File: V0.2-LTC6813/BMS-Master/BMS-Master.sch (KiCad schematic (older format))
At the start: 26 parts

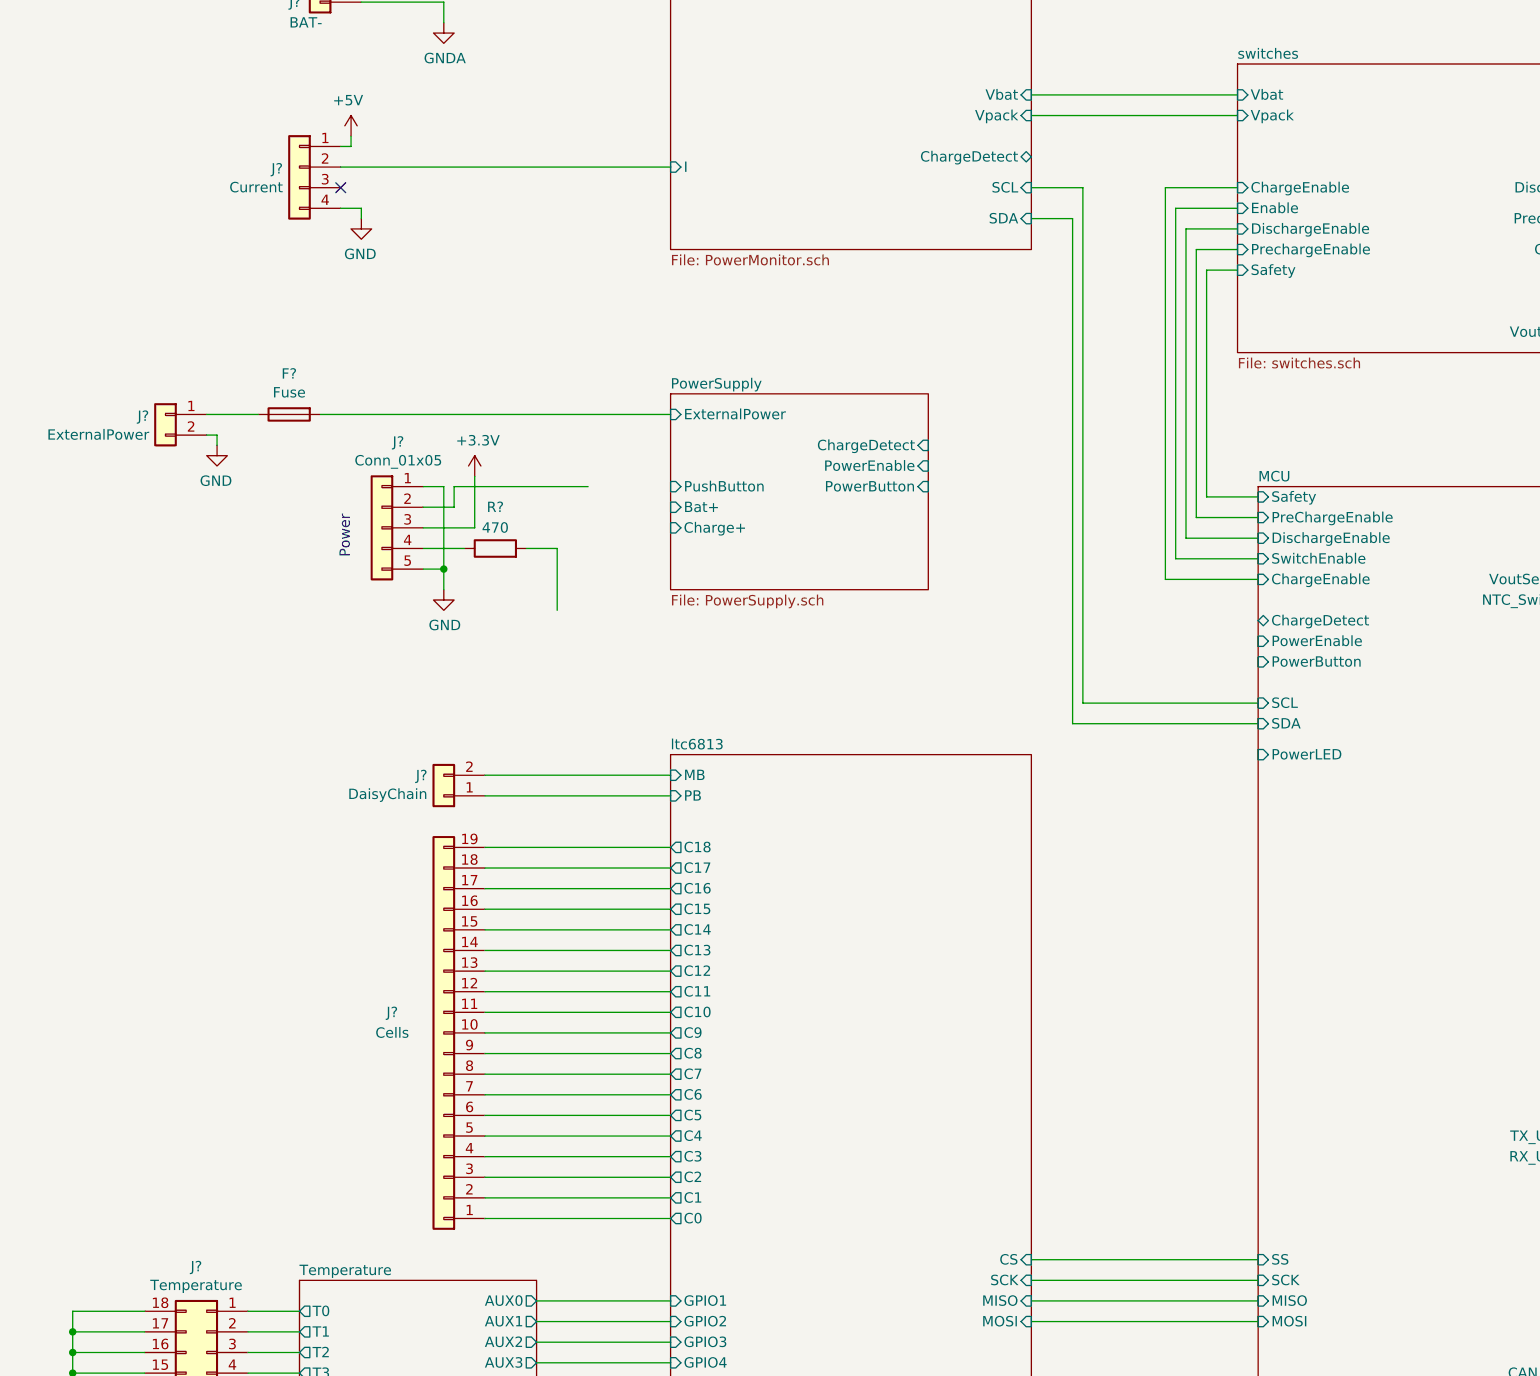
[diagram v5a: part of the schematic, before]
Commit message: Schematics 85% completed
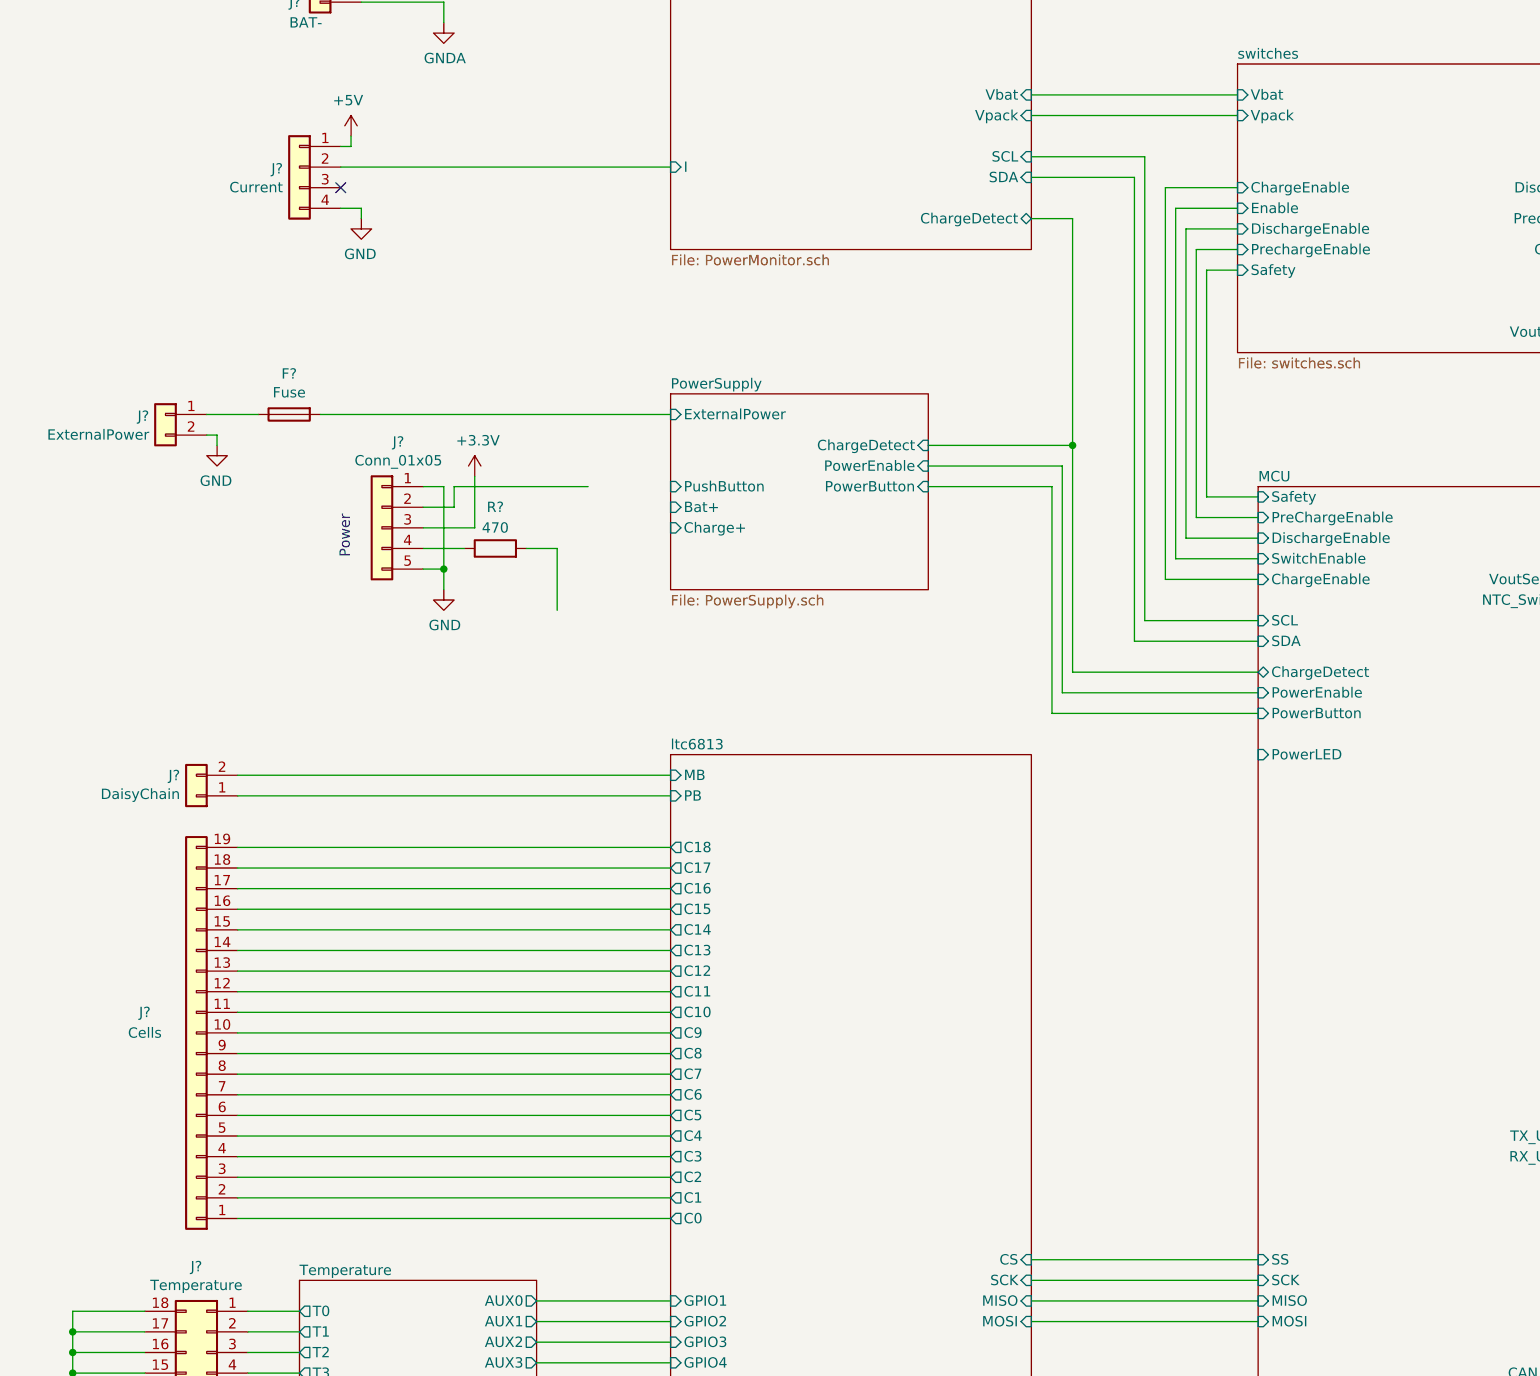
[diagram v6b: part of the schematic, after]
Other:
- moved on the sheet: DaisyChain, J?
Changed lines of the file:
@@
 L BMS-Master-rescue:Conn_01x02-Connector_Generic DaisyChain
 U 1 1 5C30CF47
-P 3250 5150
-F 0 "DaisyChain" H 3329 5142 50  0000 L CNN
-F 1 "J?" H 3329 5051 50  0000 L CNN
-F 2 "" H 3250 5150 50  0001 C CNN
-F 3 "~" H 3250 5150 50  0001 C CNN
-	1    3250 5150
+P 2050 5150
+F 0 "DaisyChain" H 2129 5142 50  0000 L CNN
+F 1 "J?" H 2129 5051 50  0000 L CNN
+F 2 "" H 2050 5150 50  0001 C CNN
+F 3 "~" H 2050 5150 50  0001 C CNN
+	1    2050 5150
 	-1   0    0    1
 $EndComp
 Wire Wire Line
-	4350 5150 3450 5150
-Wire Wire Line
-	3450 5050 4350 5050
+	4350 5150 2250 5150
+Wire Wire Line
+	2250 5050 4350 5050
 Wire Wire Line
 	10000 10300 10000 9450
@@
 F1 "PowerMonitor.sch" 50
 F2 "I" I L 4350 2100 50
-F3 "SCL" I R 6100 2200 50
-F4 "SDA" I R 6100 2350 50
+F3 "SCL" I R 6100 2050 50
+F4 "SDA" I R 6100 2150 50
 F5 "BAT+" I L 4350 900 50
 F6 "Charge+" I R 6100 950 50
@@
 F8 "Vbat" I R 6100 1750 50
 F9 "Vpack" I R 6100 1850 50
-F10 "ChargeDetect" B R 6100 2050 50
+F10 "ChargeDetect" B R 6100 2350 50
 $EndSheet
 NoConn ~ 2750 2200
@@
 L Connector_Generic:Conn_01x19 J?
 U 1 1 5C915AF7
-P 3250 6300
-F 0 "J?" H 3500 6200 50  0000 C CNN
-F 1 "Cells" H 3500 6300 50  0000 C CNN
-F 2 "" H 3250 6300 50  0001 C CNN
-F 3 "~" H 3250 6300 50  0001 C CNN
-	1    3250 6300
+P 2050 6300
+F 0 "J?" H 2300 6200 50  0000 C CNN
+F 1 "Cells" H 2300 6300 50  0000 C CNN
+F 2 "" H 2050 6300 50  0001 C CNN
+F 3 "~" H 2050 6300 50  0001 C CNN
+	1    2050 6300
 	-1   0    0    1
 $EndComp
 Wire Wire Line
-	3450 7200 4350 7200
-Wire Wire Line
-	4350 7100 3450 7100
-Wire Wire Line
-	3450 7000 4350 7000
-Wire Wire Line
-	4350 6900 3450 6900
-Wire Wire Line
-	3450 6800 4350 6800
-Wire Wire Line
-	4350 6700 3450 6700
-Wire Wire Line
-	3450 6600 4350 6600
-Wire Wire Line
-	4350 6500 3450 6500
-Wire Wire Line
-	3450 6400 4350 6400
-Wire Wire Line
-	4350 6300 3450 6300
-Wire Wire Line
-	3450 6200 4350 6200
-Wire Wire Line
-	4350 6100 3450 6100
-Wire Wire Line
-	3450 6000 4350 6000
-Wire Wire Line
-	4350 5900 3450 5900
-Wire Wire Line
-	3450 5800 4350 5800
-Wire Wire Line
-	4350 5700 3450 5700
-Wire Wire Line
-	3450 5600 4350 5600
-Wire Wire Line
-	4350 5500 3450 5500
-Wire Wire Line
-	3450 5400 4350 5400
+	2250 7200 4350 7200
+Wire Wire Line
+	4350 7100 2250 7100
+Wire Wire Line
+	2250 7000 4350 7000
+Wire Wire Line
+	4350 6900 2250 6900
+Wire Wire Line
+	2250 6800 4350 6800
+Wire Wire Line
+	4350 6700 2250 6700
+Wire Wire Line
+	2250 6600 4350 6600
+Wire Wire Line
+	4350 6500 2250 6500
+Wire Wire Line
+	2250 6400 4350 6400
+Wire Wire Line
+	4350 6300 2250 6300
+Wire Wire Line
+	2250 6200 4350 6200
+Wire Wire Line
+	4350 6100 2250 6100
+Wire Wire Line
+	2250 6000 4350 6000
+Wire Wire Line
+	4350 5900 2250 5900
+Wire Wire Line
+	2250 5800 4350 5800
+Wire Wire Line
+	4350 5700 2250 5700
+Wire Wire Line
+	2250 5600 4350 5600
+Wire Wire Line
+	4350 5500 2250 5500
+Wire Wire Line
+	2250 5400 4350 5400
 $Comp
 L power:GNDA #PWR?
@@
 F0 "MCU" 50
 F1 "MCU.sch" 50
-F2 "ChargeDetect" B L 7200 4300 50
+F2 "ChargeDetect" B L 7200 4550 50
 F3 "PreChargeEnable" I L 7200 3800 50
 F4 "DischargeEnable" I L 7200 3900 50
-F5 "PowerEnable" I L 7200 4400 50
-F6 "PowerButton" I L 7200 4500 50
+F5 "PowerEnable" I L 7200 4650 50
+F6 "PowerButton" I L 7200 4750 50
 F7 "PowerLED" I L 7200 4950 50
 F8 "LED0" I L 7200 9800 50
@@
 F20 "MOSI" I L 7200 7700 50
 F21 "SPI_WT_SS" I L 7200 9000 50
-F22 "SCL" I L 7200 4700 50
-F23 "SDA" I L 7200 4800 50
+F22 "SCL" I L 7200 4300 50
+F23 "SDA" I L 7200 4400 50
 F24 "OLED_SCL" I R 8750 8900 50
 F25 "OLED_SDA" I R 8750 9000 50
@@
 	6750 4100 7200 4100
 Wire Wire Line
-	6100 2200 6350 2200
-Wire Wire Line
-	6350 2200 6350 4700
-Wire Wire Line
-	6350 4700 7200 4700
-Wire Wire Line
-	6300 2350 6300 4800
-Wire Wire Line
-	6300 4800 7200 4800
-Wire Wire Line
-	6100 2350 6300 2350
+	6100 2050 6650 2050
+Wire Wire Line
+	6650 2050 6650 4300
+Wire Wire Line
+	6650 4300 7200 4300
+Wire Wire Line
+	6600 4400 7200 4400
 Wire Wire Line
 	6100 1750 7100 1750
@@
 Wire Wire Line
 	3700 8550 4350 8550
+Wire Wire Line
+	6600 2150 6100 2150
+Wire Wire Line
+	6600 2150 6600 4400
+Wire Wire Line
+	6100 2350 6300 2350
+Wire Wire Line
+	6300 2350 6300 3450
+Wire Wire Line
+	6300 4550 7200 4550
+Wire Wire Line
+	5600 3450 6300 3450
+Connection ~ 6300 3450
+Wire Wire Line
+	6300 3450 6300 4550
+Wire Wire Line
+	5600 3550 6250 3550
+Wire Wire Line
+	6250 3550 6250 4650
+Wire Wire Line
+	6250 4650 7200 4650
+Wire Wire Line
+	7200 4750 6200 4750
+Wire Wire Line
+	6200 4750 6200 3650
+Wire Wire Line
+	6200 3650 5600 3650
 $EndSCHEMATC

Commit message: Schematics 90% completed
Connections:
- net MCU/PowerLED: now also R?.2
- net PowerSupply/PushButton: now also J?.2 (Pin_2)
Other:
- moved on the sheet: F?, J?, R?
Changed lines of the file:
@@
 L BMS-Master-rescue:Conn_01x05-Connector_Generic J?
 U 1 1 5ABE6776
-P 2950 3850
-F 0 "J?" H 2870 4267 50  0000 C CNN
-F 1 "Conn_01x05" H 2870 4176 50  0000 C CNN
-F 2 "" H 2950 3850 50  0001 C CNN
-F 3 "~" H 2950 3850 50  0001 C CNN
-	1    2950 3850
+P 2950 4000
+F 0 "J?" H 2870 4417 50  0000 C CNN
+F 1 "Conn_01x05" H 2870 4326 50  0000 C CNN
+F 2 "" H 2950 4000 50  0001 C CNN
+F 3 "~" H 2950 4000 50  0001 C CNN
+	1    2950 4000
 	-1   0    0    -1
 $EndComp
-Text Notes 2800 4000 1    50   ~ 0
+Text Notes 2800 4150 1    50   ~ 0
 Power
 $Comp
 L BMS-Master-rescue:+3.3V-power #PWR?
 U 1 1 5ABE6960
-P 3400 3600
-F 0 "#PWR?" H 3400 3450 50  0001 C CNN
-F 1 "+3.3V" H 3415 3773 50  0000 C CNN
-F 2 "" H 3400 3600 50  0001 C CNN
-F 3 "" H 3400 3600 50  0001 C CNN
-	1    3400 3600
+P 3400 3750
+F 0 "#PWR?" H 3400 3600 50  0001 C CNN
+F 1 "+3.3V" H 3415 3923 50  0000 C CNN
+F 2 "" H 3400 3750 50  0001 C CNN
+F 3 "" H 3400 3750 50  0001 C CNN
+	1    3400 3750
 	1    0    0    -1
 $EndComp
@@
 L BMS-Master-rescue:R-Device R?
 U 1 1 5ABEC8F7
-P 3500 3950
-F 0 "R?" V 3700 3950 50  0000 C CNN
-F 1 "470" V 3600 3950 50  0000 C CNN
-F 2 "Resistors_SMD:R_0603_HandSoldering" V 3430 3950 50  0001 C CNN
-F 3 "~" H 3500 3950 50  0001 C CNN
-	1    3500 3950
+P 3500 4100
+F 0 "R?" V 3700 4100 50  0000 C CNN
+F 1 "470" V 3600 4100 50  0000 C CNN
+F 2 "Resistors_SMD:R_0603_HandSoldering" V 3430 4100 50  0001 C CNN
+F 3 "~" H 3500 4100 50  0001 C CNN
+	1    3500 4100
 	0    -1   -1   0
 $EndComp
 Wire Wire Line
-	3150 3950 3350 3950
-Wire Wire Line
-	3650 3950 3800 3950
+	3150 4100 3350 4100
+Wire Wire Line
+	3650 4100 3800 4100
 $Comp
 L BMS-Master-rescue:GND-power #PWR?
 U 1 1 5ABF492B
-P 3250 4150
-F 0 "#PWR?" H 3250 3900 50  0001 C CNN
-F 1 "GND" H 3255 3977 50  0000 C CNN
-F 2 "" H 3250 4150 50  0001 C CNN
-F 3 "" H 3250 4150 50  0001 C CNN
-	1    3250 4150
-	1    0    0    -1
-$EndComp
-Wire Wire Line
-	3150 4050 3250 4050
-Wire Wire Line
-	3250 4050 3250 4150
-Wire Wire Line
-	3250 4050 3250 3650
-Wire Wire Line
-	3250 3650 3150 3650
-Connection ~ 3250 4050
-Wire Wire Line
-	3400 3600 3400 3850
-Wire Wire Line
-	3400 3850 3150 3850
+P 3250 4300
+F 0 "#PWR?" H 3250 4050 50  0001 C CNN
+F 1 "GND" H 3255 4127 50  0000 C CNN
+F 2 "" H 3250 4300 50  0001 C CNN
+F 3 "" H 3250 4300 50  0001 C CNN
+	1    3250 4300
+	1    0    0    -1
+$EndComp
+Wire Wire Line
+	3150 4200 3250 4200
+Wire Wire Line
+	3250 4200 3250 4300
+Wire Wire Line
+	3250 4200 3250 3800
+Wire Wire Line
+	3250 3800 3150 3800
+Connection ~ 3250 4200
+Wire Wire Line
+	3400 3750 3400 4000
+Wire Wire Line
+	3400 4000 3150 4000
 $Comp
 L BMS-Master-rescue:Conn_01x04-Connector_Generic J?
@@
 F10 "Vpack" I L 7100 1850 50
 F11 "Vbat" I L 7100 1750 50
-F12 "+12V" I R 8850 2100 50
+F12 "+12V" I L 7100 2850 50
 F13 "VoutSense" I R 8850 2900 50
+F14 "NTC_Switch" I R 8850 2800 50
 $EndSheet
 Wire Wire Line
-	3800 3950 3800 4250
-Wire Wire Line
-	3150 3750 3300 3750
-Wire Wire Line
-	3300 3750 3300 3650
-Wire Wire Line
-	3300 3650 3950 3650
+	3800 4100 3800 4400
 $Comp
 L BMS-Master-rescue:Conn_01x02-Connector_Generic J?
 U 1 1 5AB7AB5E
-P 1900 3300
-F 0 "J?" H 1979 3292 50  0000 L CNN
-F 1 "ExternalPower" H 1979 3201 50  0000 L CNN
-F 2 "" H 1900 3300 50  0001 C CNN
-F 3 "~" H 1900 3300 50  0001 C CNN
-	1    1900 3300
+P 1900 3450
+F 0 "J?" H 1979 3442 50  0000 L CNN
+F 1 "ExternalPower" H 1979 3351 50  0000 L CNN
+F 2 "" H 1900 3450 50  0001 C CNN
+F 3 "~" H 1900 3450 50  0001 C CNN
+	1    1900 3450
 	-1   0    0    -1
 $EndComp
@@
 L BMS-Master-rescue:GND-power #PWR?
 U 1 1 5AB80FEA
-P 2150 3450
-F 0 "#PWR?" H 2150 3200 50  0001 C CNN
-F 1 "GND" H 2155 3277 50  0000 C CNN
-F 2 "" H 2150 3450 50  0001 C CNN
-F 3 "" H 2150 3450 50  0001 C CNN
-	1    2150 3450
+P 2150 3600
+F 0 "#PWR?" H 2150 3350 50  0001 C CNN
+F 1 "GND" H 2155 3427 50  0000 C CNN
+F 2 "" H 2150 3600 50  0001 C CNN
+F 3 "" H 2150 3600 50  0001 C CNN
+	1    2150 3600
 	-1   0    0    -1
 $EndComp
 Wire Wire Line
-	2150 3450 2150 3400
-Wire Wire Line
-	2150 3400 2100 3400
+	2150 3600 2150 3550
+Wire Wire Line
+	2150 3550 2100 3550
 $Comp
 L BMS-Master-rescue:Conn_01x02-Connector_Generic J?
@@
 L BMS-Master-rescue:Fuse-Device F?
 U 1 1 5ACF057B
-P 2500 3300
-F 0 "F?" V 2303 3300 50  0000 C CNN
-F 1 "Fuse" V 2394 3300 50  0000 C CNN
-F 2 "" V 2430 3300 50  0001 C CNN
-F 3 "~" H 2500 3300 50  0001 C CNN
-	1    2500 3300
+P 2500 3450
+F 0 "F?" V 2303 3450 50  0000 C CNN
+F 1 "Fuse" V 2394 3450 50  0000 C CNN
+F 2 "" V 2430 3450 50  0001 C CNN
+F 3 "~" H 2500 3450 50  0001 C CNN
+	1    2500 3450
 	0    -1   1    0
 $EndComp
 Wire Wire Line
-	2100 3300 2350 3300
+	2100 3450 2350 3450
 $Sheet
 S 4350 4950 1750 3750
@@
 $EndComp
 Wire Wire Line
-	4350 3300 2650 3300
+	4350 3450 2650 3450
 Wire Wire Line
 	3700 7600 4350 7600
@@
 Wire Wire Line
 	2750 2100 4350 2100
-$Sheet
-S 4350 3200 1250 950
-U 5AC18063
-F0 "PowerSupply" 50
-F1 "PowerSupply.sch" 50
-F2 "PushButton" I L 4350 3650 50
-F3 "PowerButton" I R 5600 3650 50
-F4 "PowerEnable" I R 5600 3550 50
-F5 "ExternalPower" I L 4350 3300 50
-F6 "ChargeDetect" I R 5600 3450 50
-F7 "Charge+" I L 4350 3850 50
-F8 "Bat+" I L 4350 3750 50
-$EndSheet
 Connection ~ 1450 8450
 Wire Wire Line
@@
 $EndComp
 Wire Wire Line
-	2850 900  4350 900
+	2850 900  3900 900
 Wire Wire Line
 	7200 3700 6950 3700
@@
 	6750 4100 7200 4100
 Wire Wire Line
-	6100 2050 6650 2050
-Wire Wire Line
-	6650 2050 6650 4300
-Wire Wire Line
-	6650 4300 7200 4300
-Wire Wire Line
-	6600 4400 7200 4400
+	6100 2050 6550 2050
+Wire Wire Line
+	6550 2050 6550 4300
+Wire Wire Line
+	6550 4300 7200 4300
+Wire Wire Line
+	6500 4400 7200 4400
 Wire Wire Line
 	6100 1750 7100 1750
@@
 	3700 8550 4350 8550
 Wire Wire Line
-	6600 2150 6100 2150
-Wire Wire Line
-	6600 2150 6600 4400
+	6500 2150 6100 2150
+Wire Wire Line
+	6500 2150 6500 4400
 Wire Wire Line
 	6100 2350 6300 2350
 Wire Wire Line
-	6300 2350 6300 3450
+	6300 2350 6300 3500
 Wire Wire Line
 	6300 4550 7200 4550
 Wire Wire Line
-	5600 3450 6300 3450
-Connection ~ 6300 3450
-Wire Wire Line
-	6300 3450 6300 4550
-Wire Wire Line
-	5600 3550 6250 3550
-Wire Wire Line
-	6250 3550 6250 4650
+	5600 3500 6300 3500
+Connection ~ 6300 3500
+Wire Wire Line
+	6300 3500 6300 4550
+Wire Wire Line
+	5600 3600 6250 3600
+Wire Wire Line
+	6250 3600 6250 4650
 Wire Wire Line
 	6250 4650 7200 4650
@@
 	7200 4750 6200 4750
 Wire Wire Line
-	6200 4750 6200 3650
-Wire Wire Line
-	6200 3650 5600 3650
+	6200 4750 6200 3700
+Wire Wire Line
+	6200 3700 5600 3700
+Wire Wire Line
+	5600 3300 6100 3300
+Wire Wire Line
+	6100 3300 6100 2850
+Wire Wire Line
+	6100 2850 7100 2850
+$Sheet
+S 4350 3200 1250 950
+U 5AC18063
+F0 "PowerSupply" 50
+F1 "PowerSupply.sch" 50
+F2 "PushButton" I L 4350 3900 50
+F3 "PowerButton" I R 5600 3700 50
+F4 "PowerEnable" I R 5600 3600 50
+F5 "ExternalPower" I L 4350 3450 50
+F6 "ChargeDetect" I R 5600 3500 50
+F7 "BAT+" I L 4350 3300 50
+F8 "+12V" I R 5600 3300 50
+F9 "EnableFromExt" I R 5600 3400 50
+$EndSheet
+Wire Wire Line
+	4350 3300 3900 3300
+Wire Wire Line
+	3900 3300 3900 900
+Connection ~ 3900 900
+Wire Wire Line
+	3900 900  4350 900
+Wire Wire Line
+	3800 4400 6150 4400
+Wire Wire Line
+	6150 4400 6150 4950
+Wire Wire Line
+	6150 4950 7200 4950
+Wire Wire Line
+	3150 3900 4350 3900
+Wire Wire Line
+	5600 3400 9150 3400
+Wire Wire Line
+	9150 3400 9150 6700
+Wire Wire Line
+	9150 6700 9250 6700
+Wire Wire Line
+	9150 6700 9150 7800
+Wire Wire Line
+	9150 7800 9250 7800
+Connection ~ 9150 6700
+Wire Wire Line
+	8750 4100 9000 4100
+Wire Wire Line
+	9000 4100 9000 2900
+Wire Wire Line
+	9000 2900 8850 2900
+Wire Wire Line
+	8850 2800 9050 2800
+Wire Wire Line
+	9050 2800 9050 4200
+Wire Wire Line
+	9050 4200 8750 4200
 $EndSCHEMATC
